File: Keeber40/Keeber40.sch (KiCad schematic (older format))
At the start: 81 parts, among them K1 KEYSW, K10 KEYSW, K11 KEYSW, K12 KEYSW, K13 KEYSW, K14 KEYSW, K15 KEYSW, K16 KEYSW, K17 KEYSW, K18 KEYSW, K19 KEYSW, K2 KEYSW, K20 KEYSW, K21 KEYSW, K22 KEYSW, K23 KEYSW, K24 KEYSW, K25 KEYSW, K26 KEYSW, K27 KEYSW, K28 KEYSW, K29 KEYSW, K3 KEYSW, K30 KEYSW, K31 KEYSW, K32 KEYSW, K33 KEYSW, K34 KEYSW, K35 KEYSW, K36 KEYSW, K37 KEYSW, K38 KEYSW, K39 KEYSW, K4 KEYSW, K5 KEYSW, K6 KEYSW, K7 KEYSW, K8 KEYSW, K9 KEYSW, SW1 SW_PUSH, U1 Pico

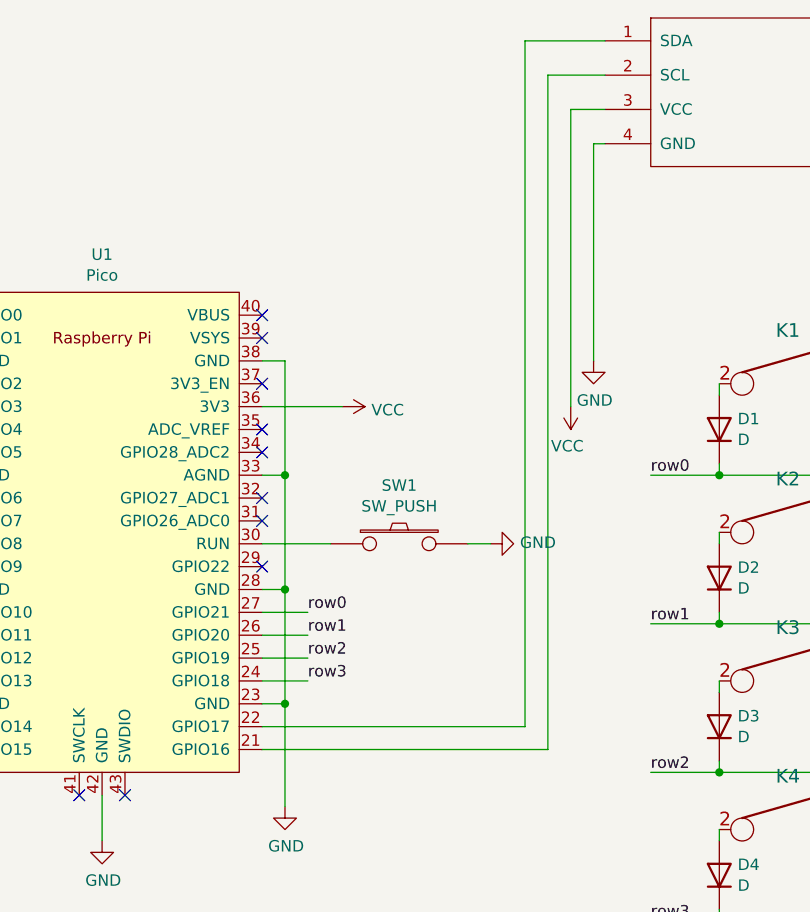
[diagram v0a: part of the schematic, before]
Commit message: fixed pcb oled traces
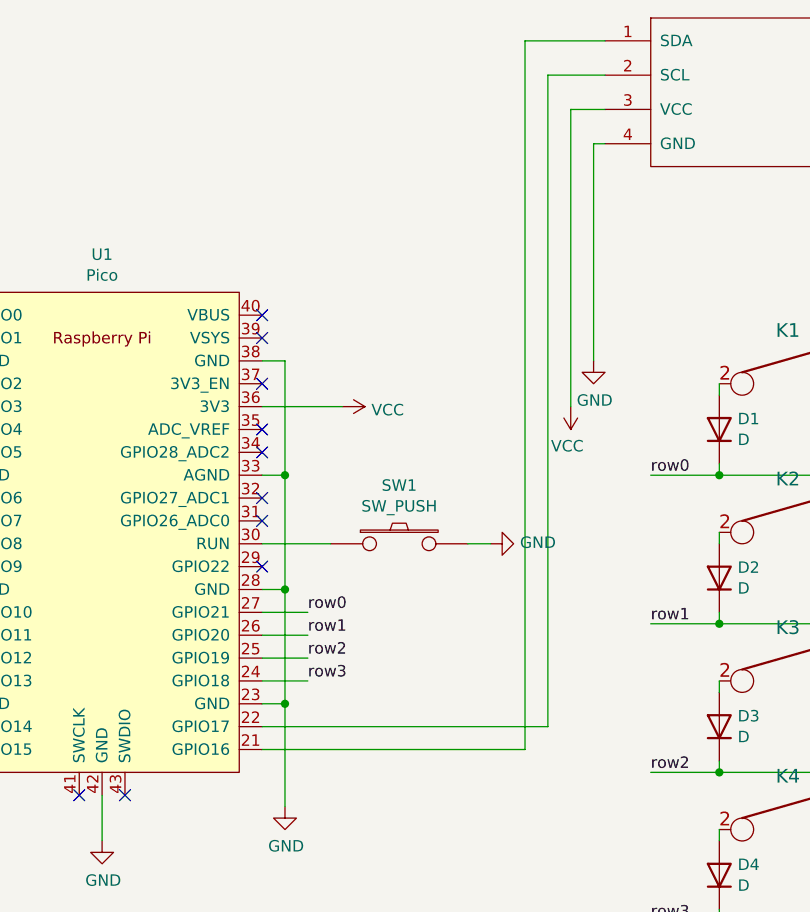
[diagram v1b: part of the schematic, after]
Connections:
- net at U1.21 (GPIO16): now also OL1.1 (SDA); no longer OL1.2 (SCL)
- net at U1.22 (GPIO17): now also OL1.2 (SCL); no longer OL1.1 (SDA)
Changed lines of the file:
@@
 	3700 1350 3700 2650
 Wire Wire Line
-	2350 4150 3600 4150
-Wire Wire Line
 	3600 1200 3850 1200
-Wire Wire Line
-	2350 4050 3500 4050
-Wire Wire Line
-	3500 4050 3500 1050
 Wire Wire Line
 	3500 1050 3850 1050
@@
 $EndComp
 Wire Wire Line
-	3600 1200 3600 4150
+	2350 4150 3500 4150
+Wire Wire Line
+	3500 1050 3500 4150
+Wire Wire Line
+	3600 1200 3600 4050
+Wire Wire Line
+	3600 4050 2350 4050
 $EndSCHEMATC
